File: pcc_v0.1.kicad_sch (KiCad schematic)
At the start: 57 parts, among them J1 Conn_01x02_Socket, J2 Conn_01x04_Socket, J3 Conn_01x02_Socket, J4 Conn_02x14_Counter_Clockwise, J5 Conn_01x06_Socket, J7 Conn_01x04_Socket, J8 Conn_01x02_Socket, J9 Conn_01x02_Socket, K1 G9KB-1A_DC12, K3 PCN-112D3MHZ_000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

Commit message: next round of edits
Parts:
- removed J5: Conn_01x06_Socket, Connector_Molex:Molex_Mini-Fit_Jr_5566-06A2_2x03_P4.20mm_Vertical, symbol Connector:Conn_01x06_Socket
- added J6: Conn_01x04_Socket, Connector_Molex:Molex_Mini-Fit_Jr_5566-04A2_2x02_P4.20mm_Vertical, symbol Connector:Conn_01x04_Socket
- added R30, R31: R, Resistor_SMD:R_0805_2012Metric, symbol Device:R_Small_US
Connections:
- net B+_out is gone; now on net GNDS: R21.1, R28.1
- net B+_in: now also J6.2 (Pin_2)
- net CANRX: now also R30.1; no longer U8.4 (R)
- net CANTX: now also R31.2; no longer U8.1 (D)
- net GLV-: no longer U8.8 (Rs)
- net GNDS: now also J6.1 (Pin_1)
- net TS+: now also J6.4 (Pin_4)
- net TS-: now also J6.3 (Pin_3)
- new net: R30.2, U8.4 (R)
- new net: R31.1, U8.1 (D)
- no-connect marks 71 -> 69
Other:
- moved on the sheet: R28

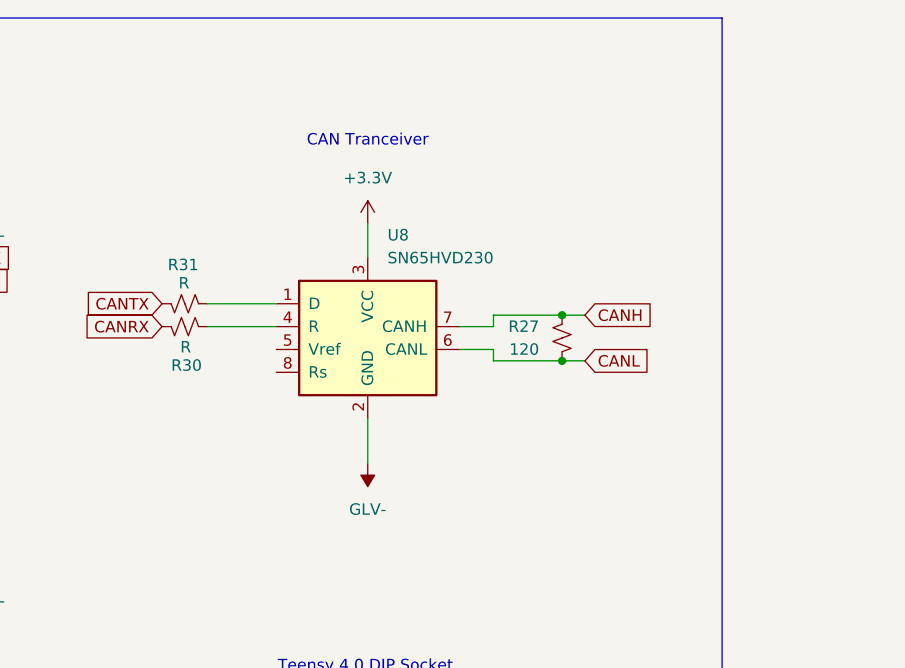
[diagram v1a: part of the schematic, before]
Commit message: can tranceiver filtering stuff
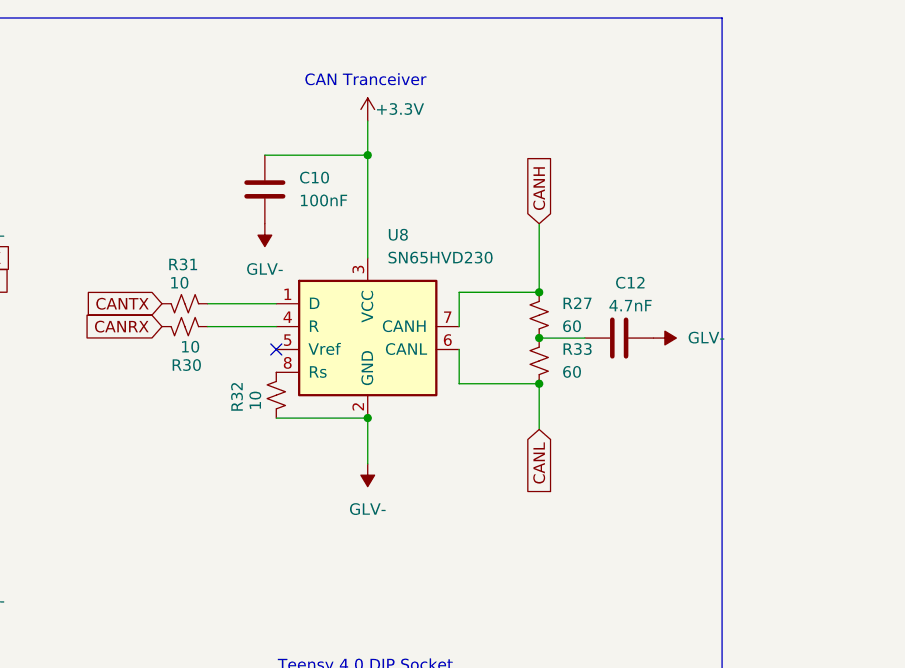
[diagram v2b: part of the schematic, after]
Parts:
- added C10: 100nF, Capacitor_SMD:C_0805_2012Metric, symbol Device:C
- added C12: 4.7nF, Capacitor_SMD:C_0805_2012Metric, symbol Device:C
- added R32: 10, Resistor_SMD:R_0805_2012Metric, symbol Device:R_Small_US
- added R33: 60, Resistor_SMD:R_0805_2012Metric, symbol Device:R_Small_US
- R27: value 120 -> 60
- R30, R31: value R -> 10
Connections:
- net +3.3V: now also C10.1
- net CANL: now also R33.2; no longer R27.2
- net GLV-: now also C10.2, C12.2, R32.2
- net at U8.8 (Rs): now also R32.1
- new net: C12.1, R27.2, R33.1
- no-connect marks 69 -> 70
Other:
- moved on the sheet: R27

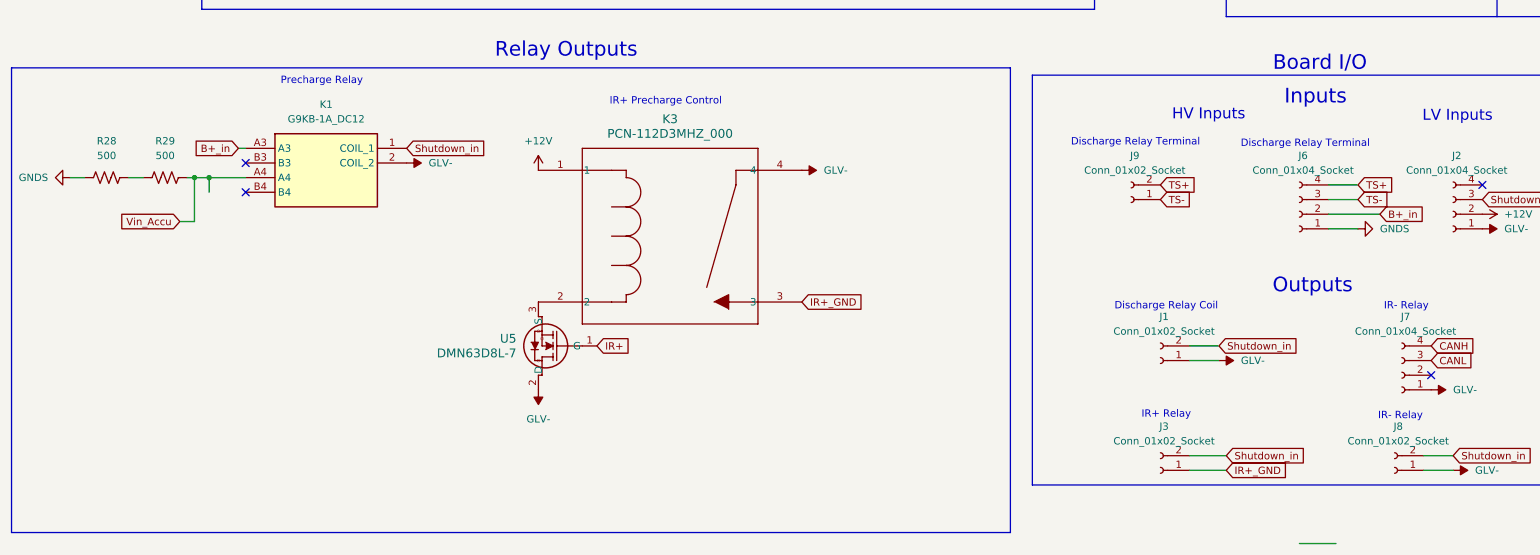
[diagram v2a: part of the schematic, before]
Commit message: added discharge relay
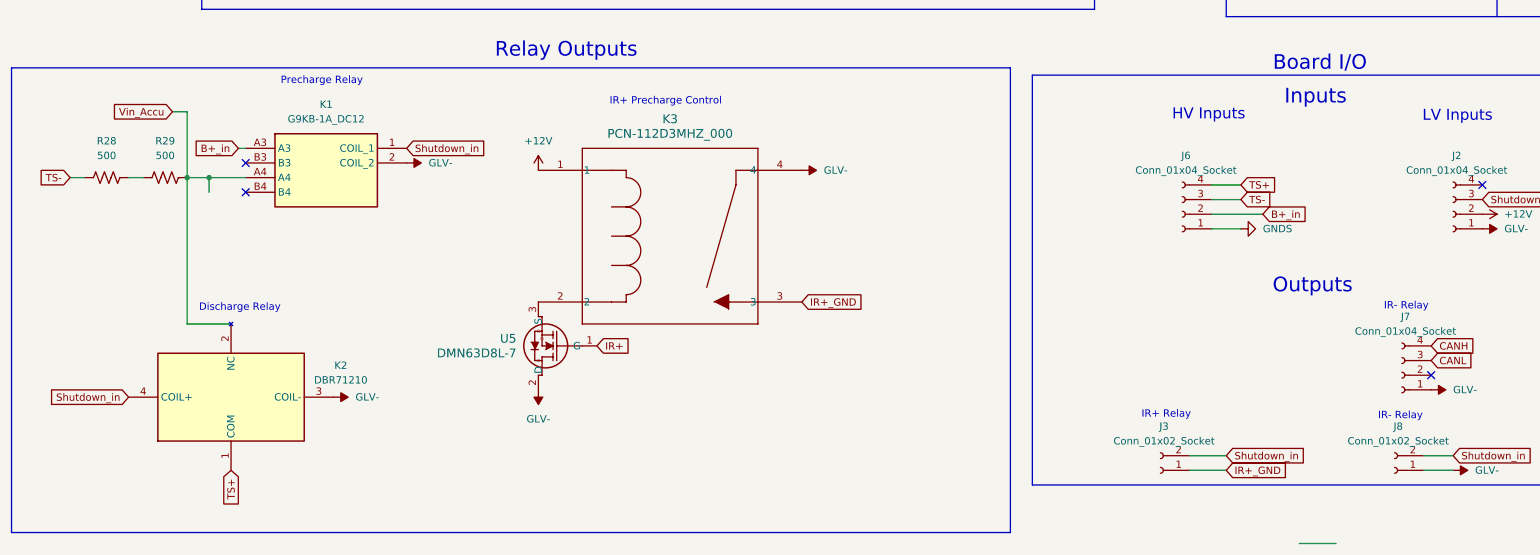
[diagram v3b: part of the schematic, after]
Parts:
- removed J1, J9: Conn_01x02_Socket, Connector_Molex:Molex_Mini-Fit_Jr_5566-02A2_2x01_P4.20mm_Vertical, symbol Connector:Conn_01x02_Socket
- added K2: DBR71210, discharge relay:DBR71210, symbol DBR71210:DBR71210
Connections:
- net GLV-: now also K2.3 (COIL-)
- net GNDS: no longer R28.1
- net Shutdown_in: now also K2.4 (COIL+)
- net TS+: now also K2.1 (COM)
- net TS-: now also R28.1
- net Vin_Accu: now also K2.2 (NC)
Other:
- note added: "Discharge Relay"
- note removed: "Discharge Relay Coil"
- note removed: "Discharge Relay Terminal"
- moved on the sheet: J6

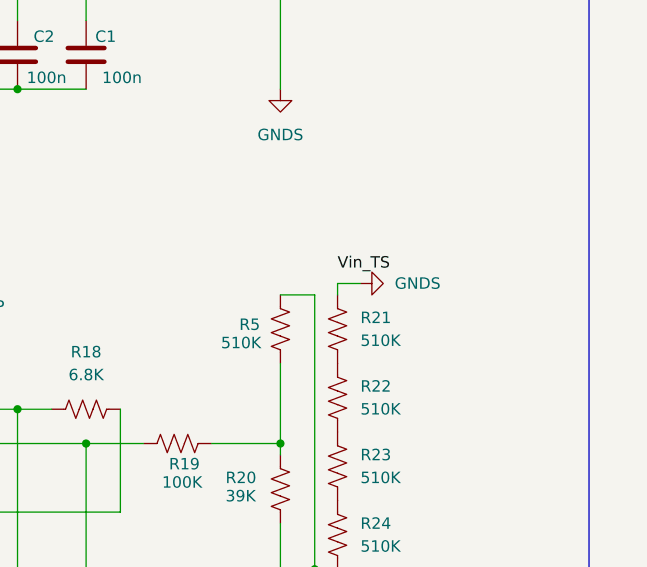
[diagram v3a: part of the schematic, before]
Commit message: fixed text placement
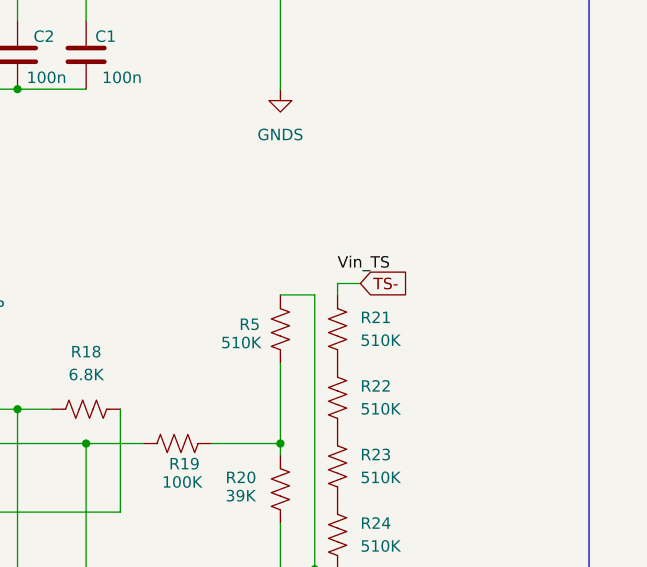
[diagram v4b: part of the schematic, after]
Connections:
- net GNDS: no longer R21.1
- net TS-: now also R21.1
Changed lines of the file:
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@@
 		)
 	)
+	(global_label "TS-"
+		(shape input)
+		(at 360.68 97.79 0)
+		(fields_autoplaced yes)
+		(effects
+			(font
+				(size 1.27 1.27)
+			)
+			(justify left)
+		)
+		(property "Intersheetrefs" "${INTERSHEET_REFS}"
+			(at 367.4147 97.79 0)
+			(effects
+				(font
+					(size 1.27 1.27)
+				)
+				(justify left)
+				(hide yes)
+			)
+		)
+	)
 	(global_label "CANRX"
 		(shape input)
@@
 		(length 2.54)
 		(shape round)
-		(at 227.33 186.69 90)
-		(effects
-			(font
-				(size 1.27 1.27)
-			)
-			(justify left bottom)
-		)
-		(property "Netclass" "precharge"
-			(at 219.71 185.166 0)
-			(effects
-				(font
-					(size 1.27 1.27)
-					(italic yes)
-				)
-				(justify left)
-			)
-		)
-	)
-	(netclass_flag ""
-		(length 2.54)
-		(shape round)
 		(at 82.55 172.72 0)
 		(fields_autoplaced yes)
@@
 					(unit 1)
 				)
-			)
-		)
-	)
-	(symbol
-		(lib_id "power:GNDS")
-		(at 360.68 97.79 90)
-		(unit 1)
-		(exclude_from_sim no)
-		(in_bom yes)
-		(on_board yes)
-		(dnp no)
-		(fields_autoplaced yes)
-		(property "Reference" "#PWR043"
-			(at 367.03 97.79 0)
-			(effects
-				(font
-					(size 1.27 1.27)
-				)
-				(hide yes)
-			)
-		)
-		(property "Value" "GNDS"
-			(at 364.49 97.7899 90)
-			(effects
-				(font
-					(size 1.27 1.27)
-				)
-				(justify right)
-			)
-		)
-		(property "Footprint" ""
-			(at 360.68 97.79 0)
-			(effects
-				(font
-					(size 1.27 1.27)
-				)
-				(hide yes)
-			)
-		)
-		(property "Datasheet" ""
-			(at 360.68 97.79 0)
-			(effects
-				(font
-					(size 1.27 1.27)
-				)
-				(hide yes)
-			)
-		)
-		(property "Description" "Power symbol creates a global label with name \"GNDS\" , signal ground"
-			(at 360.68 97.79 0)
-			(effects
-				(font
-					(size 1.27 1.27)
-				)
-				(hide yes)
-			)
-		)
-		(pin "1"
-		)
-		(instances
-			(project "pcc_v0.1"
-				(path "/cd50b4df-2796-417a-bb78-7e5b371bc4af"
-					(reference "#PWR043")
-					(unit 1)
-				)

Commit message: generated bom
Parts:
- C10: value 100nF -> 100n
- C12: value 4.7nF -> 4.7n
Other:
- moved on the sheet: J3, J7, J8
